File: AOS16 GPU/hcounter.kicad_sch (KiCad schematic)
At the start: 22 parts, among them U10 74LS30, U11 74LS30, U12 74HC00, U13 74AHC04, U14 74LS30, U15 74LS30, U16 74LS30, U17 74LS30, U4 74LS161, U5 74LS161, U6 74AHC04, U7 74AHC04, U8 74LS30, U9 74LS30

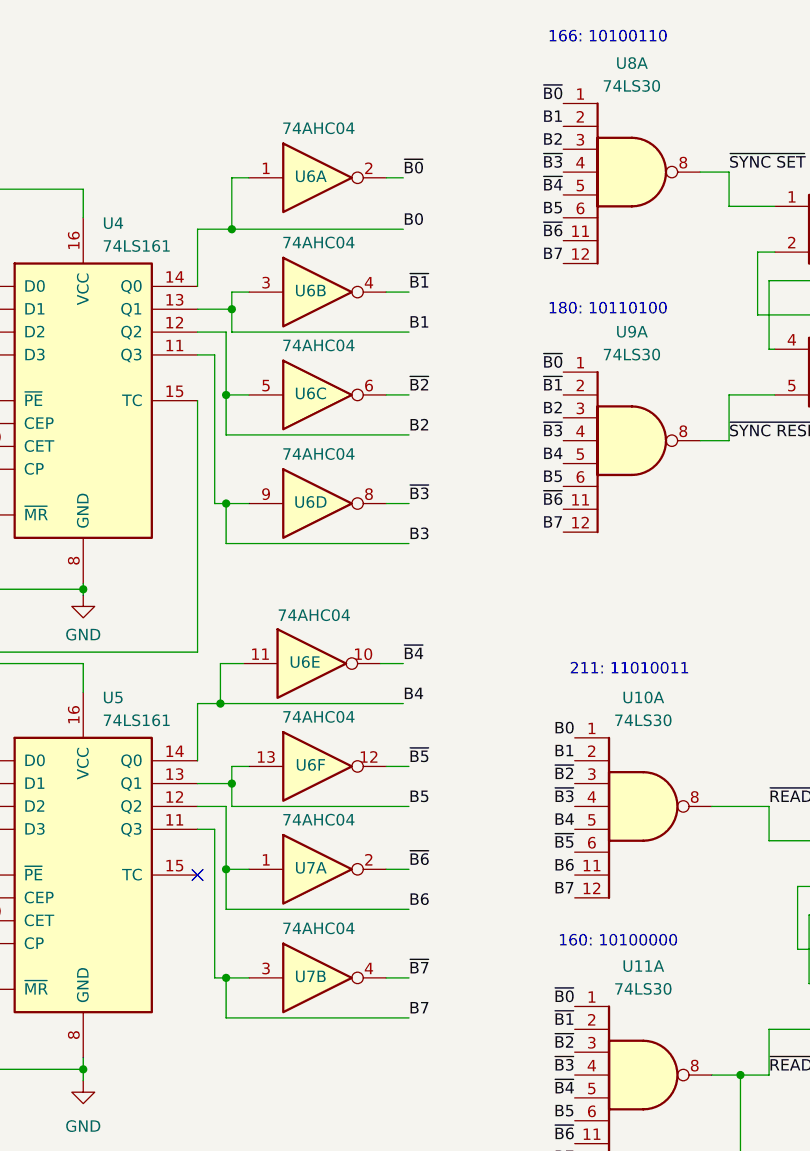
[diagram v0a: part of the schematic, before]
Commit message: Migrated to KiCad 9.0 and made changes to GPU
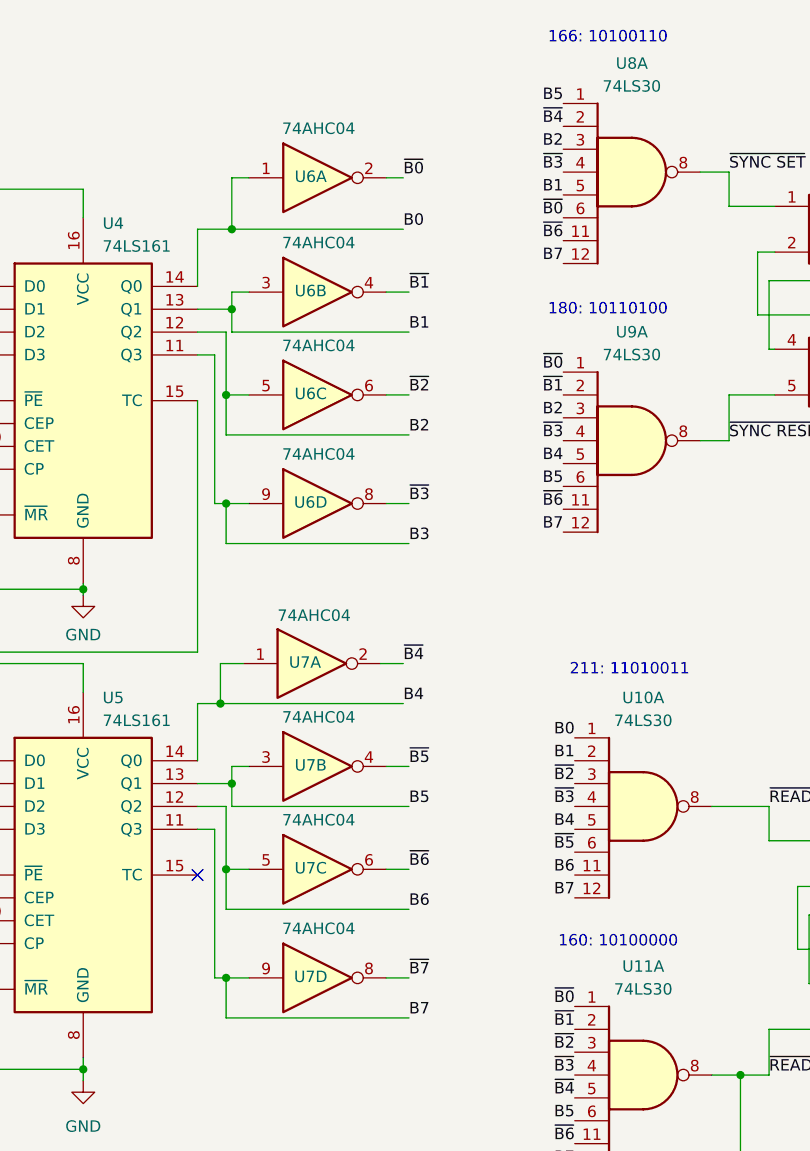
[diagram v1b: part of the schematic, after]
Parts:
- renumbered U6 to U7
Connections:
- net B1: now also U8.5; no longer U8.2
- net B4: now also U7.1; no longer U7.11
- net B5: now also U7.3, U8.1; no longer U7.13, U8.6
- net B6: now also U7.5; no longer U7.1
- net B7: now also U7.9; no longer U7.3
- net ~{B0}: now also U8.6; no longer U8.1
- net ~{B4}: now also U7.2, U8.2; no longer U7.10, U8.5
- net ~{B5}: now also U7.4; no longer U7.12
- net ~{B6}: now also U7.6; no longer U7.2
- net ~{B7}: now also U7.8; no longer U7.4
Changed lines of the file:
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@@
 		)
 	)
-	(label "~{B4}"
-		(at 105.41 40.64 180)
+	(label "~{B0}"
+		(at 105.41 43.18 180)
 		(effects
 			(font
@@
 		)
 	)
-	(label "~{B0}"
-		(at 105.41 30.48 180)
-		(effects
-			(font
-				(size 1.27 1.27)
-			)
-			(justify right bottom)
-		)
-	)
 	(label "B1"
 		(at 106.68 103.505 180)
@@
 		)
 	)
-	(label "B1"
-		(at 105.41 33.02 180)
-		(effects
-			(font
-				(size 1.27 1.27)
-			)
-			(justify right bottom)
-		)
-	)
 	(label "B5"
 		(at 106.68 143.51 180)
@@
 		)
 	)
+	(label "B1"
+		(at 105.41 40.64 180)
+		(effects
+			(font
+				(size 1.27 1.27)
+			)
+			(justify right bottom)
+		)
+	)
 	(label "B5"
-		(at 105.41 43.18 180)
+		(at 105.41 30.48 180)
 		(effects
 			(font
@@
 		)
 	)
+	(label "~{B4}"
+		(at 105.41 33.02 180)
+		(effects
+			(font
+				(size 1.27 1.27)
+			)
+			(justify right bottom)
+		)
+	)
 	(label "B2"
 		(at 220.98 33.02 180)
@@
 		(lib_id "74xx:74AHC04")
 		(at 78.105 104.14 0)
-		(unit 6)
+		(unit 2)
 		(exclude_from_sim no)
 		(in_bom yes)
 		(on_board yes)
 		(dnp no)
-		(property "Reference" "U6"
+		(property "Reference" "U7"
 			(at 77.343 104.013 0)
 			(effects
@@
 			(project "AOS16 GPU"
 				(path "/30867551-fb5e-4d50-9b6f-10252ea432a0/4bf792ca-1e03-422d-88f5-eccf37716806"
-					(reference "U6")
-					(unit 6)
+					(reference "U7")
+					(unit 2)
 				)
 			)
@@
 		(lib_id "74xx:74AHC04")
 		(at 78.105 115.57 0)
-		(unit 1)
+		(unit 3)
 		(exclude_from_sim no)
 		(in_bom yes)
@@
 				(path "/30867551-fb5e-4d50-9b6f-10252ea432a0/4bf792ca-1e03-422d-88f5-eccf37716806"
 					(reference "U7")
-					(unit 1)
+					(unit 3)
 				)
 			)
@@
 		(lib_id "74xx:74AHC04")
 		(at 77.47 92.71 0)
-		(unit 5)
+		(unit 1)
 		(exclude_from_sim no)
 		(in_bom yes)
 		(on_board yes)
 		(dnp no)
-		(property "Reference" "U6"
+		(property "Reference" "U7"
 			(at 76.708 92.583 0)
 			(effects
@@
 			(project "AOS16 GPU"
 				(path "/30867551-fb5e-4d50-9b6f-10252ea432a0/4bf792ca-1e03-422d-88f5-eccf37716806"
-					(reference "U6")
-					(unit 5)
+					(reference "U7")
+					(unit 1)
 				)
 			)
@@
 		(lib_id "74xx:74AHC04")
 		(at 78.105 127.635 0)
-		(unit 2)
+		(unit 4)
 		(exclude_from_sim no)
 		(in_bom yes)
@@
 				(path "/30867551-fb5e-4d50-9b6f-10252ea432a0/4bf792ca-1e03-422d-88f5-eccf37716806"
 					(reference "U7")
-					(unit 2)
+					(unit 4)
 				)
 			)

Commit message: GPU PCB Design v1
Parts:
- removed unit 4 of U7
- added C27: 0.1uF, Capacitor_SMD:C_0603_1608Metric, symbol Device:C
- added unit 5 of U11
- renumbered C11 to C10, C12 to C11, C13 to C12, C14 to C13, C15 to C14, C8 to C7, C9 to C8, C10 to C9, U11 to U10, U12 to U11, U13 to U12, U14 to U13, U15 to U14, U16 to U15, U17 to U16, U4 to U3, U5 to U4, U6 to U5, U7 to U5, U8 to U7, U9 to U8, U10 to U9
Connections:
- net +5V: now also C27.1, U11.14 (VCC)
- net B0: now also U5.11; no longer U5.1, U9.1
- net B1: now also U6.1; no longer U6.3, U7.5, U9.2
- net B2: now also U6.3, U8.12; no longer U6.5, U7.3, U8.3
- net B3: now also U6.5, U7.11; no longer U6.9
- net B4: now also U8.11, U9.12; no longer U8.5, U9.5
- net B5: now also U10.1, U7.3, U8.4; no longer U10.6, U7.1, U8.6
- net B7: now also U10.3, U7.2, U8.5, U9.5; no longer U10.12, U7.12, U8.12, U9.12
- net GND: now also C27.2, U11.7 (GND)
- net ~{B0}: now also U10.2, U5.10, U7.5, U8.2, U9.6; no longer U10.1, U5.2, U7.6, U8.1
- net ~{B1}: now also U10.6, U6.2, U7.6, U8.1, U9.2; no longer U10.2, U6.4, U8.2
- net ~{B2}: now also U10.5, U6.4, U7.1; no longer U10.3, U6.6
- net ~{B3}: now also U6.6, U8.6; no longer U6.8, U7.4, U8.4
- net ~{B4}: now also U10.11, U7.12; no longer U10.5, U7.2
- net ~{B5}: now also U9.1; no longer U9.6
- net ~{B6}: now also U10.12, U7.4, U8.3; no longer U10.11, U7.11, U8.11
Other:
- note added: "168: 10101000"
- note added: "208: 11010000"
- note removed: "166: 10100110"
- note removed: "211: 11010011"

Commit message: updated gpu
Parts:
- added D2, D5: LED_Small, LED_SMD:LED_0603_1608Metric, symbol Device:LED_Small
- added R1, R41: 220, Resistor_SMD:R_0603_1608Metric, symbol Device:R_Small
- U10: renamed from U16; value 74LS30 -> 74HC30
- U10, U7, U8, U9: value 74LS30 -> 74HC30
- U3, U4: value 74LS161 -> 74HC161
- U7: renamed from U13; value 74LS30 -> 74HC30
- U8: renamed from U14; value 74LS30 -> 74HC30
- U9: renamed from U15; value 74LS30 -> 74HC30
- renumbered U12 to U5
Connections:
- net ~{READ SET} is gone; now on net LINE_END: U11.9, U9.8
- net B1: now also U7.11
- net B2: now also U7.1, U8.6; no longer U8.12
- net B3: now also U7.6, U8.1; no longer U7.11
- net GND: now also U3.3 (D0), U3.4 (D1), U3.5 (D2), U3.6 (D3), U4.3 (D0), U4.4 (D1), U4.5 (D2), U4.6 (D3), D2.1 (K), D5.1 (K)
- net HSync: now also R41.1
- net LINE_END: now also R1.1; no longer U10.8, U11.13
- net ~{B1}: now also U8.12; no longer U7.6, U8.1
- net ~{B2}: no longer U7.1
- net ~{B3}: no longer U8.6
- new net: D5.2 (A), R41.2
- new net: D2.2 (A), R1.2
- new net ~{READ RESET}: U10.8, U11.13
- no-connect marks 10 -> 2
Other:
- note added: "174: 10101110"
- note added: "188: 10111100"
- note removed: "168: 10101000"
- note removed: "180: 10110100"
- moved on the sheet: U11A, U11B, U7A, U8A
